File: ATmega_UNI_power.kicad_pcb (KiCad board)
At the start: 2 copper layers, 16.3 x 22.9 mm, 11 parts, among them J1 Barrel_Jack_MountingPin, J9 Power_Conn, J91 RAW_Conn, J92 RAW_Conn, U33 AMS1117-3.3, U55 AMS1117-5.0

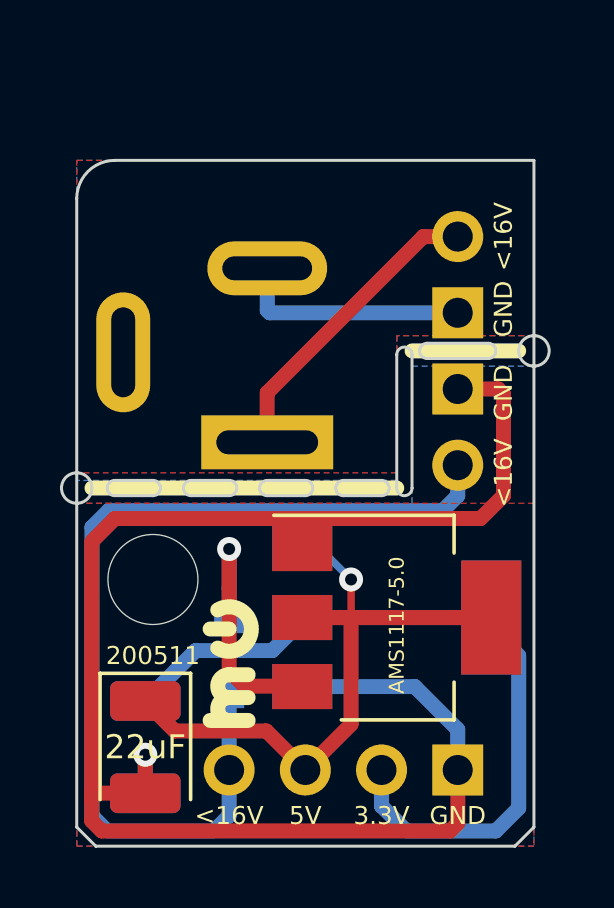
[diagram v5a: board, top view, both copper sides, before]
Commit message: bigger raw bridge holes
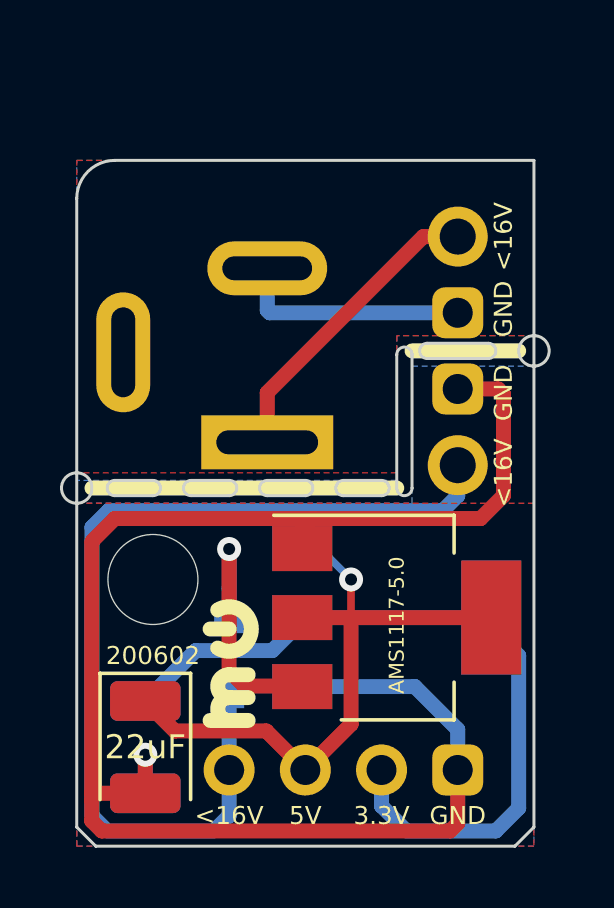
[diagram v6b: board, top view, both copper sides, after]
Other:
- board text added: "200602"
- board text removed: "200511"
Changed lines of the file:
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@@
   )
   (setup
-    (last_trace_width 0.5)
+    (last_trace_width 0.25)
     (user_trace_width 0.25)
     (user_trace_width 0.5)
@@
     (pad 2 thru_hole oval (at 0 2.54 270) (size 1.7 1.7) (drill 1) (layers *.Cu *.Mask)
       (net 4 3.3V))
-    (pad 1 thru_hole rect (at 0 0 270) (size 1.7 1.7) (drill 1) (layers *.Cu *.Mask)
+    (pad 1 thru_hole roundrect (at 0 0 270) (size 1.7 1.7) (drill 1) (layers *.Cu *.Mask) (roundrect_rratio 0.25)
       (net 2 GND))
     (model ${KISYS3DMOD}/Connector_PinSocket_2.54mm.3dshapes/PinSocket_1x04_P2.54mm_Vertical.wrl
@@
       (effects (font (size 1 1) (thickness 0.15)))
     )
-    (pad 1 thru_hole rect (at 0 0) (size 1.7 1.7) (drill 1) (layers *.Cu *.Mask)
+    (pad 1 thru_hole roundrect (at 0 0) (size 1.7 1.7) (drill 1) (layers *.Cu *.Mask) (roundrect_rratio 0.25)
       (net 2 GND))
-    (pad 2 thru_hole oval (at 0 2.54) (size 1.7 1.7) (drill 1) (layers *.Cu *.Mask)
+    (pad 2 thru_hole oval (at 0 2.54) (size 2 2) (drill 1.2) (layers *.Cu *.Mask)
       (net 5 RAW_JACK))
     (model ${KISYS3DMOD}/Connector_PinHeader_2.54mm.3dshapes/PinHeader_1x02_P2.54mm_Vertical.wrl
@@
       (effects (font (size 1 1) (thickness 0.15)))
     )
-    (pad 1 thru_hole rect (at 0 0 180) (size 1.7 1.7) (drill 1) (layers *.Cu *.Mask)
+    (pad 1 thru_hole roundrect (at 0 0 180) (size 1.7 1.7) (drill 1) (layers *.Cu *.Mask) (roundrect_rratio 0.25)
       (net 6 "Net-(J1-Pad2)"))
-    (pad 2 thru_hole oval (at 0 2.54 180) (size 1.7 1.7) (drill 1) (layers *.Cu *.Mask)
+    (pad 2 thru_hole oval (at 0 2.54 180) (size 2 2) (drill 1.2) (layers *.Cu *.Mask)
       (net 7 "Net-(J1-Pad1)"))
     (model ${KISYS3DMOD}/Connector_PinHeader_2.54mm.3dshapes/PinHeader_1x02_P2.54mm_Vertical.wrl
@@
   )
   (gr_line (start 157.48 65.405) (end 158.115 66.04) (layer Edge.Cuts) (width 0.1))
-  (gr_text 200511 (at 159.512 59.69) (layer B.SilkS)
+  (gr_text 200602 (at 159.512 59.69) (layer B.SilkS)
     (effects (font (size 0.6 0.6) (thickness 0.125)) (justify mirror))
   )
@@
   )
   (gr_line (start 172.085 66.04) (end 172.72 65.405) (layer Edge.Cuts) (width 0.1))
-  (gr_text 200511 (at 160.02 59.69) (layer F.SilkS)
-    (effects (font (size 0.6 0.6) (thickness 0.125)))
-  )
+  (gr_text 200602 (at 160.02 59.69) (layer F.SilkS)
+    (effects (font (size 0.6 0.6) (thickness 0.125)))
+  )
